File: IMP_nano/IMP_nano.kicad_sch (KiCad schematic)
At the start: 33 parts, among them J1 DG301, J2 Holes, Q1 BC547, Q2 AO3400A, SW1 SW_DPST_x2, SW2 SW_DIP_x04, U1 STM32L051C8T6

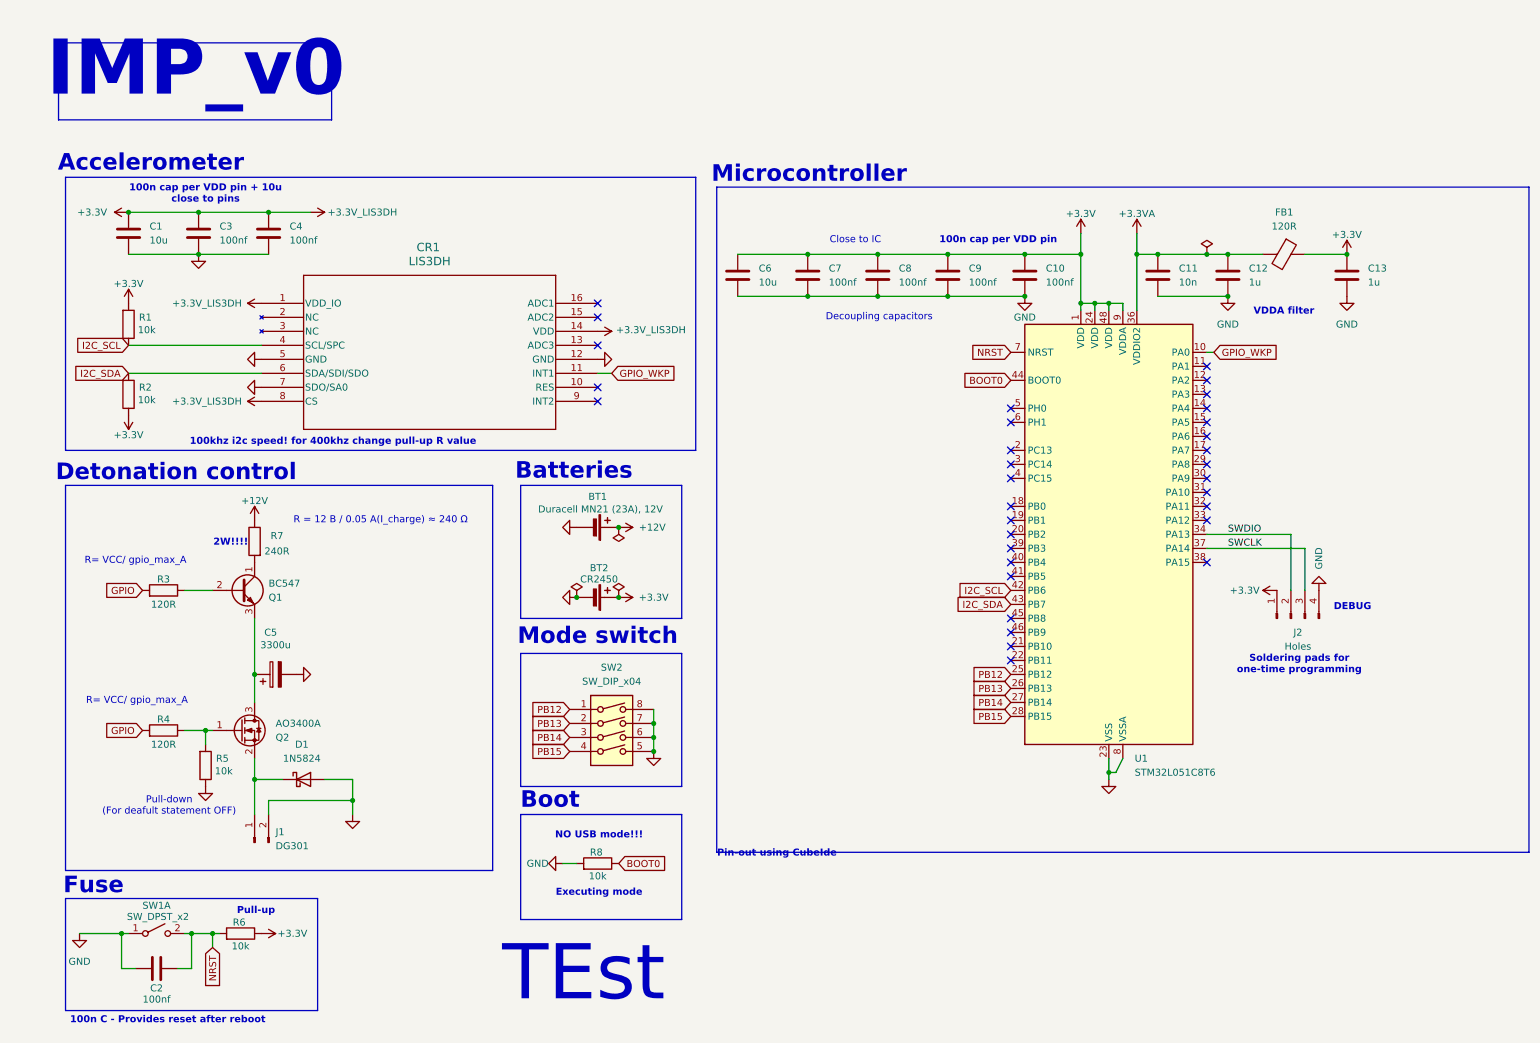
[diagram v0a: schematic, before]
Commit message: Schematic update + footprint assignment + 3d models
-Buzzer added
-23/1/26
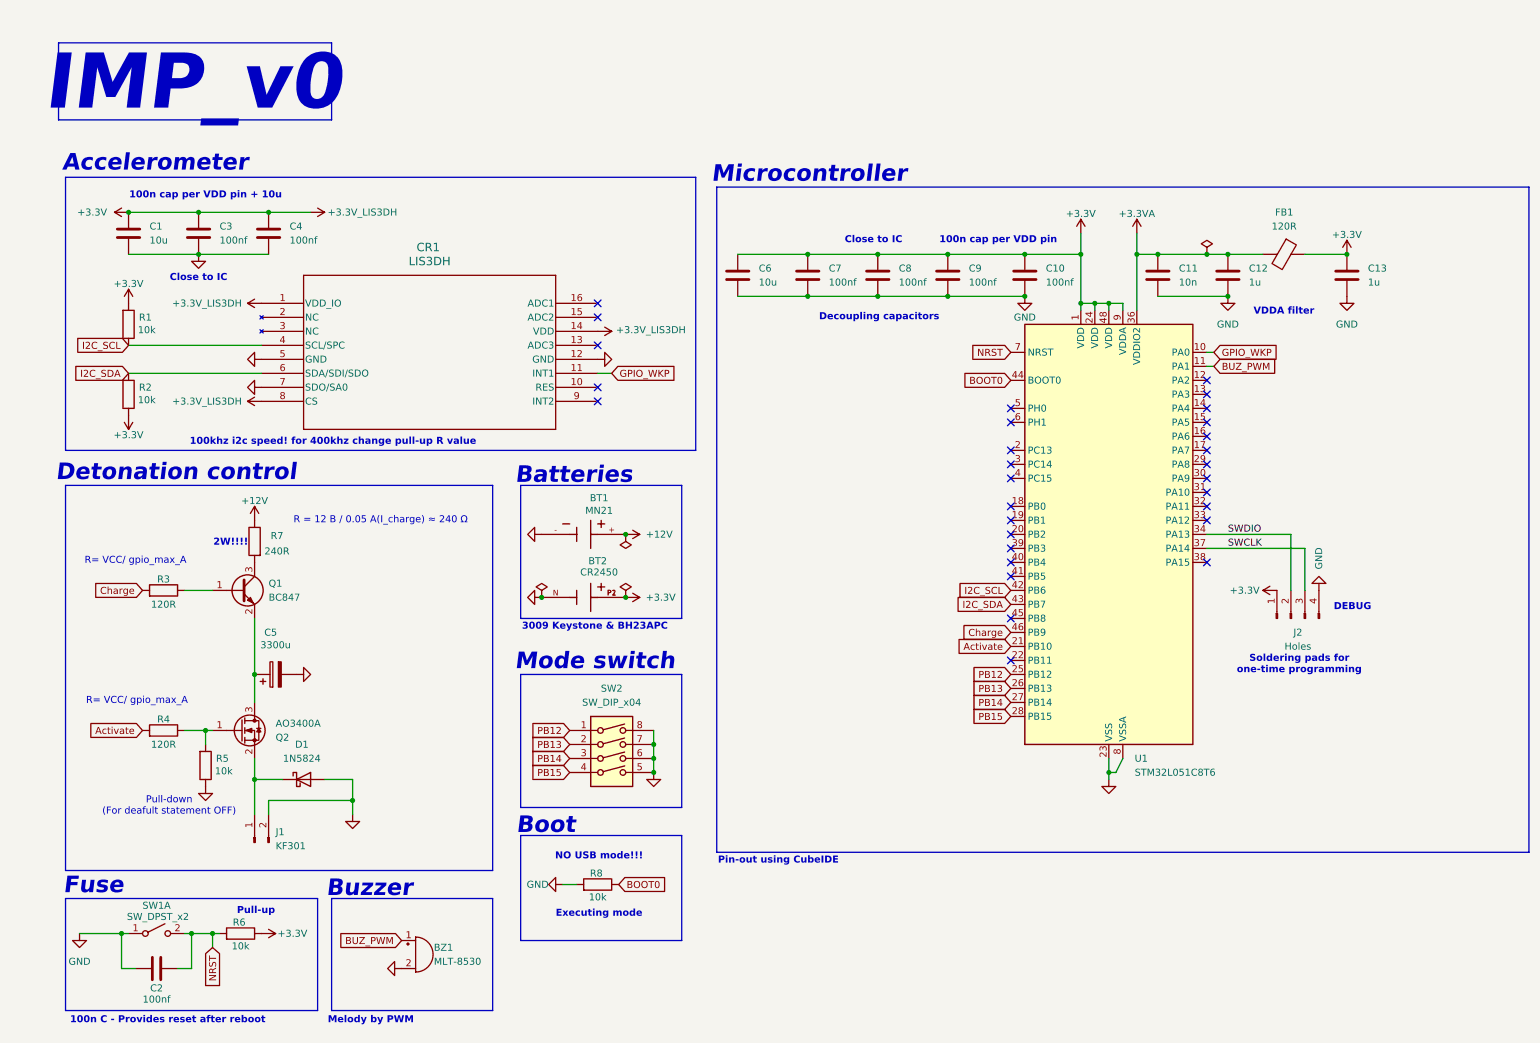
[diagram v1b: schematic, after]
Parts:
- removed BT1: Duracell MN21 (23A), 12V, IMP_LIB:duracell mn21 (a23) 12v holder, symbol Device:Battery_Cell
- removed BT2: СR2450, symbol Device:Battery_Cell
- removed Q1: BC547, Package_TO_SOT_THT:TO-92_Inline, symbol Transistor_BJT:BC547
- added BT1: MN21, IMP_LIB:BAT_BH23APC, symbol IMP_LIB_SYM:BH23APC
- added BT2: CR2450, IMP_LIB:BAT_3009, symbol CR2450 holder:3009
- added BZ1: MLT-8530, IMP_LIB:MLT-8530_JHE, symbol Device:Buzzer
- added Q1: BC847, Package_TO_SOT_SMD:SOT-23, symbol Transistor_BJT:BC847
- D1: footprint Diode_THT:D_DO-201AD_P15.24mm_Horizontal -> Diode_SMD:D_SMA
- J1: value DG301 -> KF301; footprint (none) -> IMP_LIB:HANDSON_KF301-2P
- R7: footprint Resistor_THT:R_Axial_DIN0207_L6.3mm_D2.5mm_P15.24mm_Horizontal -> IMP_LIB:RESC6432X90N
- SW1: footprint Button_Switch_SMD:SW_SPST_CK_RS282G05A3 -> Button_Switch_THT:SW_XKB_DM1-16UP-1
- SW2: footprint Button_Switch_SMD:SW_DIP_SPSTx04_Slide_9.78x12.34mm_W8.61mm_P2.54mm -> IMP_LIB:SW_A6S-4101-H_OMR
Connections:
- net +12V: now also BT1.+
- net +3.3V: now also BT2.P1, BT2.P2
- net GND: now also BT1.-, BT2.N, BZ1.2 (-)
- net BUZ_PWM: now reaches U1.11 (PA1)
- net BUZ_PWM: now also BZ1.1 (+)
- net Activate: now reaches U1.21 (PB10)
- net Activate: now also R4.2
- net Charge: now reaches U1.46 (PB9)
- net Charge: now also R3.2
- net at R3.1: now also Q1.1 (B)
- net at R7.2: now also Q1.3 (C)
- net at C5.1, Q2.3 (D): now also Q1.2 (E)
- removed net GPIO: R3.2, R4.2
- no-connect marks 33 -> 30
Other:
- note added: "100n cap per VDD pin + 10u"
- note added: "3009 Keystone & BH23APC"
- note added: "Buzzer"
- note added: "Melody by PWM"
- note added: "Pin-out using CubeIDE"
- note removed: "100n cap per VDD pin + 10u close to pins"
- note removed: "Pin-out using CubeIde"
- note removed: "TEst"
- moved on the sheet: R8, SW2

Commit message: precomplete of back side of pcb
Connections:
- no-connect marks 30 -> 32
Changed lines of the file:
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@@
+	)
+	(no_connect
+		(at 50.8 66.04)
 	)
 	(no_connect
@@
 	)
 	(no_connect
+		(at 50.8 68.58)
+	)
+	(no_connect

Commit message: PCB - placed all components - added filled copper zones(back - GND, front - 3v3)   SCHEMATIC - corrected mode switch
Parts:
- added R10, R11, R12, R9: 10k, Resistor_SMD:R_01005_0402Metric, symbol Device:R
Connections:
- net +3.3V: now also SW2.5, SW2.6, SW2.7, SW2.8
- net GND: now also R10.1, R11.1, R12.1, R9.1; no longer SW2.5, SW2.6, SW2.7, SW2.8
- net PB12: now also R12.2
- net PB13: now also R11.2
- net PB14: now also R10.2
- net PB15: now also R9.2
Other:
- moved on the sheet: R8, SW2

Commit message: Reapply "Merge branch 'main' of https://github.com/VM789/Iniciator_LIS3DH_STM32L051"
This reverts commit 2ad7139c444b11e79b7e6934f4438ad5f06415cd.
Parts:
- SW2: value SW_DIP_x04 -> DIP_x04
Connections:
- net PB13 is gone; now on net PB12: R11.2, SW2.2, U1.26 (PB13)
- net PB15 is gone; now on net PB14: R9.2, SW2.4, U1.28 (PB15)
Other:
- moved on the sheet: R10, R11, R12, R9

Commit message: Revert "Small schematic edition"
This reverts commit bbe39c2e898aba73dfbb216a0e94a96616dd3fc8.
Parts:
- SW2: value DIP_x04 -> SW_DIP_x04
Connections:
- net PB12: no longer R11.2, SW2.2, U1.26 (PB13)
- net PB14: no longer R9.2, SW2.4, U1.28 (PB15)
- new net PB13: R11.2, SW2.2, U1.26 (PB13)
- new net PB15: R9.2, SW2.4, U1.28 (PB15)
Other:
- moved on the sheet: R10, R11, R12, R9

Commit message: update pcb & schematic
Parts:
- added H1, H2, H3: MountingHole_Pad, symbol Mechanical:MountingHole_Pad
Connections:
- net 12v_OUT: now reaches D1.1 (K), J1.1 (Pin_1), Q2.2 (S)
- net 12v_C5: now reaches C5.1, Q1.2 (E), Q2.3 (D)
- net 12v_R7: now reaches Q1.3 (C), R7.2
- net +12V renamed 12v
- net PB12 renamed M_PB15
- net M_PB15: now also U1.28 (PB15); no longer U1.25 (PB12)
- net PB13 renamed M_PB14
- net M_PB14: now also U1.27 (PB14); no longer U1.26 (PB13)
- net PB14 renamed M_PB13
- net M_PB13: now also U1.26 (PB13); no longer U1.27 (PB14)
- net PB15 renamed M_PB12
- net M_PB12: now also U1.25 (PB12); no longer U1.28 (PB15)
- no-connect marks 32 -> 35
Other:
- note removed: "2W!!!!"
- moved on the sheet: R7

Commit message: fully made pcb & update schematic
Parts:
- removed H1, H2, H3: MountingHole_Pad, symbol Mechanical:MountingHole_Pad
- C1, C10, C11, C12, C13, C2, C3, C4, C6, C7, C8, C9: footprint Capacitor_SMD:C_01005_0402Metric -> Capacitor_SMD:C_0201_0603Metric
- R1, R10, R11, R12, R2, R3, R4, R5, R6, R8, R9: footprint Resistor_SMD:R_01005_0402Metric -> Resistor_SMD:R_0201_0603Metric
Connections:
- no-connect marks 35 -> 32

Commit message: corrected pcb & schematic
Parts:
- added R13: 120R, Resistor_SMD:R_0201_0603Metric, symbol Device:R
- J2: value Holes -> SH1.04PIN
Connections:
- net BUZ_PWM: now also R13.2; no longer BZ1.1 (+)
- new net: BZ1.1 (+), R13.1
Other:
- moved on the sheet: BZ1
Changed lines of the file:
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@@
 	(wire
 		(pts
-			(xy 116.84 105.41) (xy 123.19 105.41)
+			(xy 64.77 180.34) (xy 73.66 180.34)
 		)
 		(stroke
@@
 	(wire
 		(pts
-			(xy 24.13 71.12) (xy 26.67 71.12)
+			(xy 116.84 105.41) (xy 123.19 105.41)
 		)
 		(stroke
@@
 	(wire
 		(pts
-			(xy 177.8 123.19) (xy 186.69 123.19)
+			(xy 24.13 71.12) (xy 26.67 71.12)
 		)
 		(stroke
@@
 	(wire
 		(pts
-			(xy 207.01 64.77) (xy 207.01 63.5)
+			(xy 177.8 123.19) (xy 186.69 123.19)
 		)
 		(stroke
@@
 	(wire
 		(pts
-			(xy 39.37 54.61) (xy 26.67 54.61)
+			(xy 207.01 64.77) (xy 207.01 63.5)
 		)
 		(stroke
@@
 	(wire
 		(pts
-			(xy 64.77 179.07) (xy 76.2 179.07)
+			(xy 39.37 54.61) (xy 26.67 54.61)
 		)
 		(stroke
@@
 	)
 	(label "BUZ_PWM"
-		(at 64.77 179.07 0)
+		(at 64.77 180.34 0)
 		(effects
 			(font
@@
 			)
 		)
-		(property "Value" "Holes"
+		(property "Value" "SH1.04PIN"
 			(at 238.76 125.73 90)
 			(effects
@@
 	)
 	(symbol
+		(lib_id "Device:R")
+		(at 77.47 180.34 270)
+		(mirror x)
+		(unit 1)
+		(exclude_from_sim no)
+		(in_bom yes)
+		(on_board yes)
+		(dnp no)
+		(property "Reference" "R13"
+			(at 77.47 178.308 90)
+			(effects
+				(font
+					(size 1.27 1.27)
+				)
+			)
+		)
+		(property "Value" "120R"
+			(at 77.47 182.88 90)
+			(effects
+				(font
+					(size 1.27 1.27)
+				)
+			)
+		)
+		(property "Footprint" "Resistor_SMD:R_0201_0603Metric"
+			(at 77.47 182.118 90)
+			(effects
+				(font
+					(size 1.27 1.27)
+				)
+				(hide yes)
+			)
+		)
+		(property "Datasheet" "~"
+			(at 77.47 180.34 0)
+			(effects
+				(font
+					(size 1.27 1.27)
+				)
+				(hide yes)
+			)
+		)
+		(property "Description" "Resistor"
+			(at 77.47 180.34 0)
+			(effects
+				(font
+					(size 1.27 1.27)
+				)
+				(hide yes)
+			)
+		)
+		(pin "2"
+		)
+		(pin "1"
+		)
+		(instances
+			(project "IMP_nano"
+				(path "/1380bf0b-ebcf-4197-8419-e21f84722079"
+					(reference "R13")
+					(unit 1)
+				)
+			)
+		)
+	)
+	(symbol
 		(lib_id "power:+3.3V")
 		(at 50.8 81.28 90)
@@
 	(symbol
 		(lib_id "power:GND")
-		(at 76.2 184.15 270)
+		(at 81.28 185.42 270)
 		(unit 1)
 		(exclude_from_sim no)
@@
 		(fields_autoplaced yes)
 		(property "Reference" "#PWR016"
-			(at 69.85 184.15 0)
+			(at 74.93 185.42 0)
 			(effects
 				(font
@@
 		)
 		(property "Value" "GND"
-			(at 71.12 184.15 0)
+			(at 76.2 185.42 0)
 			(effects
 				(font
@@
 		)
 		(property "Footprint" ""
-			(at 76.2 184.15 0)
+			(at 81.28 185.42 0)
 			(effects
 				(font
@@
 		)
 		(property "Datasheet" ""
-			(at 76.2 184.15 0)
+			(at 81.28 185.42 0)
 			(effects
 				(font
@@
 		)
 		(property "Description" "Power symbol creates a global label with name \"GND\" , ground"
-			(at 76.2 184.15 0)
+			(at 81.28 185.42 0)
 			(effects
 				(font
@@
 	(symbol
 		(lib_id "Device:Buzzer")
-		(at 78.74 181.61 0)
+		(at 83.82 182.88 0)
 		(unit 1)
 		(exclude_from_sim no)
@@
 		(dnp no)
 		(property "Reference" "BZ1"
-			(at 82.042 180.34 0)
+			(at 87.63 184.912 0)
 			(effects
 				(font
@@
 		)
 		(property "Value" "MLT-8530"
-			(at 82.042 182.88 0)
+			(at 81.534 187.706 0)
 			(effects
 				(font
@@
 		)
 		(property "Footprint" "IMP_LIB:MLT-8530_JHE"
-			(at 78.105 179.07 90)
+			(at 83.185 180.34 90)
 			(effects
 				(font
@@
 		)
 		(property "Datasheet" "~"
-			(at 78.105 179.07 90)
+			(at 83.185 180.34 90)
 			(effects
 				(font
@@
 		)
 		(property "Description" "Buzzer, polarized"
-			(at 78.74 181.61 0)
+			(at 83.82 182.88 0)
 			(effects
 				(font
